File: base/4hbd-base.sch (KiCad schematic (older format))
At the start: 13 parts, among them J1 Screw_Terminal_01x03, J10 Screw_Terminal_01x04, J11 Screw_Terminal_01x02, J12 Conn_01x03, J13 Conn_01x08, J2 Screw_Terminal_01x03, J3 Screw_Terminal_01x03, J4 Screw_Terminal_01x03, J5 Screw_Terminal_01x02, J6 Screw_Terminal_01x02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

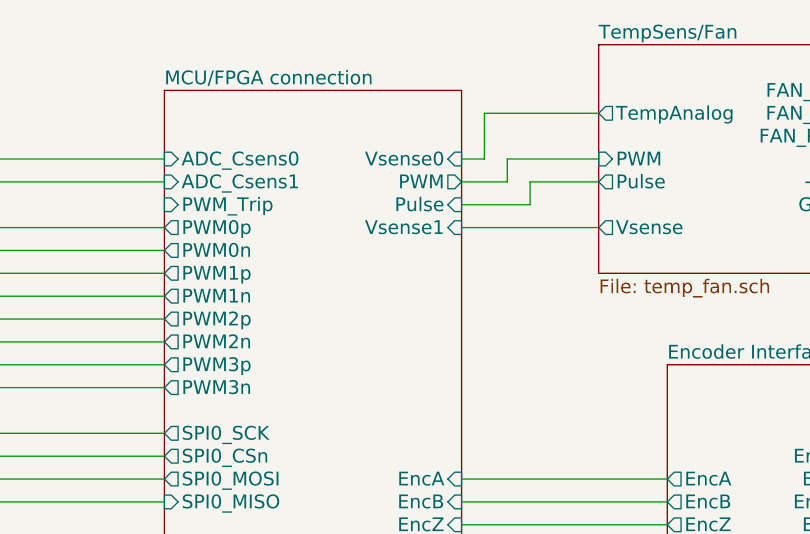
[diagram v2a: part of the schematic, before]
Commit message: Update base board: 1. Add extra analog voltage input to core board.   -> update pinmux 2. Assign most footprints. 3. Generate netlist. 4. Add core_sf board. 5. Add kicad_symbols library submodule.
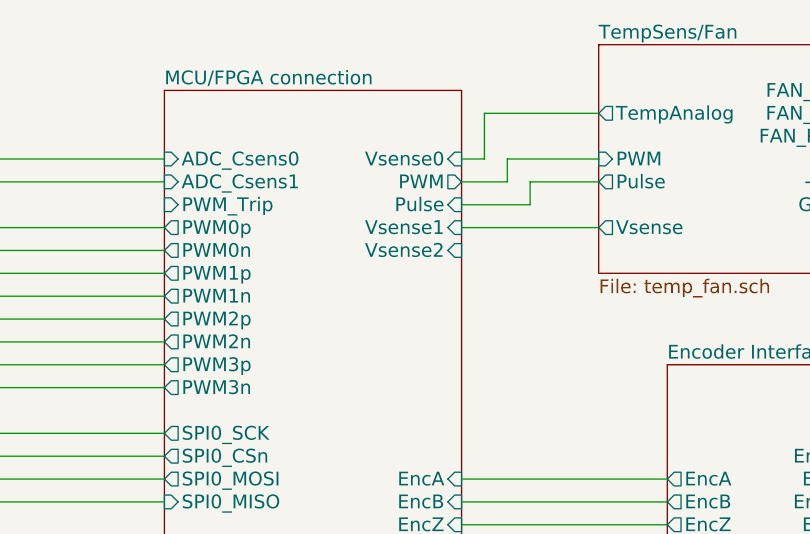
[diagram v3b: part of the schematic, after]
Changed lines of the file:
@@
 F40 "ADC_Csens1" I L 6900 1400 60
 F41 "ADC_Csens0" I L 6900 1300 60
+F42 "Vsense2" I R 8200 1700 60
 $EndSheet
 $Sheet
@@
 $EndSheet
 $Comp
-L GNDD #PWR8
+L GNDD #PWR01
 U 1 1 5A1C4DF7
 P 8900 6000
-F 0 "#PWR8" H 8900 5750 50  0001 C CNN
+F 0 "#PWR01" H 8900 5750 50  0001 C CNN
 F 1 "GNDD" H 8900 5875 50  0000 C CNN
 F 2 "" H 8900 6000 50  0001 C CNN
@@
 $EndComp
 $Comp
-L GNDD #PWR7
+L GNDD #PWR02
 U 1 1 5A1C5052
 P 8900 3500
-F 0 "#PWR7" H 8900 3250 50  0001 C CNN
+F 0 "#PWR02" H 8900 3250 50  0001 C CNN
 F 1 "GNDD" H 8900 3375 50  0000 C CNN
 F 2 "" H 8900 3500 50  0001 C CNN
@@
 $EndComp
 $Comp
-L GNDD #PWR5
+L GNDD #PWR03
 U 1 1 5A1C5445
 P 4800 5600
-F 0 "#PWR5" H 4800 5350 50  0001 C CNN
+F 0 "#PWR03" H 4800 5350 50  0001 C CNN
 F 1 "GNDD" H 4800 5475 50  0000 C CNN
 F 2 "" H 4800 5600 50  0001 C CNN
@@
 $EndComp
 $Comp
-L GNDD #PWR4
+L GNDD #PWR04
 U 1 1 5A1C7749
 P 4800 3800
-F 0 "#PWR4" H 4800 3550 50  0001 C CNN
+F 0 "#PWR04" H 4800 3550 50  0001 C CNN
 F 1 "GNDD" H 4800 3675 50  0000 C CNN
 F 2 "" H 4800 3800 50  0001 C CNN
@@
 $EndComp
 $Comp
-L GNDD #PWR6
+L GNDD #PWR05
 U 1 1 5A1D2700
 P 8400 4800
-F 0 "#PWR6" H 8400 4550 50  0001 C CNN
+F 0 "#PWR05" H 8400 4550 50  0001 C CNN
 F 1 "GNDD" H 8400 4675 50  0000 C CNN
 F 2 "" H 8400 4800 50  0001 C CNN
@@
 $EndComp
 $Comp
-L GNDD #PWR10
+L GNDD #PWR06
 U 1 1 5A1D7E7F
 P 10500 5500
-F 0 "#PWR10" H 10500 5250 50  0001 C CNN
+F 0 "#PWR06" H 10500 5250 50  0001 C CNN
 F 1 "GNDD" H 10500 5375 50  0000 C CNN
 F 2 "" H 10500 5500 50  0001 C CNN
@@
 $EndComp
 $Comp
-L GNDD #PWR11
+L GNDD #PWR07
 U 1 1 5A1E3D1F
 P 10600 2500
-F 0 "#PWR11" H 10600 2250 50  0001 C CNN
+F 0 "#PWR07" H 10600 2250 50  0001 C CNN
 F 1 "GNDD" H 10600 2375 50  0000 C CNN
 F 2 "" H 10600 2500 50  0001 C CNN
@@
 $EndComp
 $Comp
-L GNDD #PWR9
+L GNDD #PWR08
 U 1 1 5A1E950D
 P 10200 1600
-F 0 "#PWR9" H 10200 1350 50  0001 C CNN
+F 0 "#PWR08" H 10200 1350 50  0001 C CNN
 F 1 "GNDD" H 10200 1475 50  0000 C CNN
 F 2 "" H 10200 1600 50  0001 C CNN
@@
 	1200 7000 1400 7000
 $Comp
-L GNDPWR #PWR3
+L GNDPWR #PWR09
 U 1 1 5A1F43A1
 P 2800 5600
-F 0 "#PWR3" H 2800 5400 50  0001 C CNN
+F 0 "#PWR09" H 2800 5400 50  0001 C CNN
 F 1 "GNDPWR" H 2800 5470 50  0000 C CNN
 F 2 "" H 2800 5550 50  0001 C CNN
@@
 $EndComp
 $Comp
-L GNDPWR #PWR1
+L GNDPWR #PWR010
 U 1 1 5A1F4674
 P 1200 7100
-F 0 "#PWR1" H 1200 6900 50  0001 C CNN
+F 0 "#PWR010" H 1200 6900 50  0001 C CNN
 F 1 "GNDPWR" H 1200 6970 50  0000 C CNN
 F 2 "" H 1200 7050 50  0001 C CNN
@@
 $EndComp
 $Comp
-L GNDPWR #PWR2
+L GNDPWR #PWR011
 U 1 1 5A1F4ECF
 P 2800 3600
-F 0 "#PWR2" H 2800 3400 50  0001 C CNN
+F 0 "#PWR011" H 2800 3400 50  0001 C CNN
 F 1 "GNDPWR" H 2800 3470 50  0000 C CNN
 F 2 "" H 2800 3550 50  0001 C CNN
@@
 	6200 7200 6200 7400
 $Comp
-L GNDD #PWR?
+L GNDD #PWR012
 U 1 1 5A3B40B0
 P 6200 7400
-F 0 "#PWR?" H 6200 7150 50  0001 C CNN
+F 0 "#PWR012" H 6200 7150 50  0001 C CNN
 F 1 "GNDD" H 6200 7275 50  0000 C CNN
 F 2 "" H 6200 7400 50  0001 C CNN
@@
 $EndComp
 $Comp
-L GNDD #PWR?
+L GNDD #PWR013
 U 1 1 5A3B43A6
 P 4600 7000
-F 0 "#PWR?" H 4600 6750 50  0001 C CNN
+F 0 "#PWR013" H 4600 6750 50  0001 C CNN
 F 1 "GNDD" H 4600 6875 50  0000 C CNN
 F 2 "" H 4600 7000 50  0001 C CNN

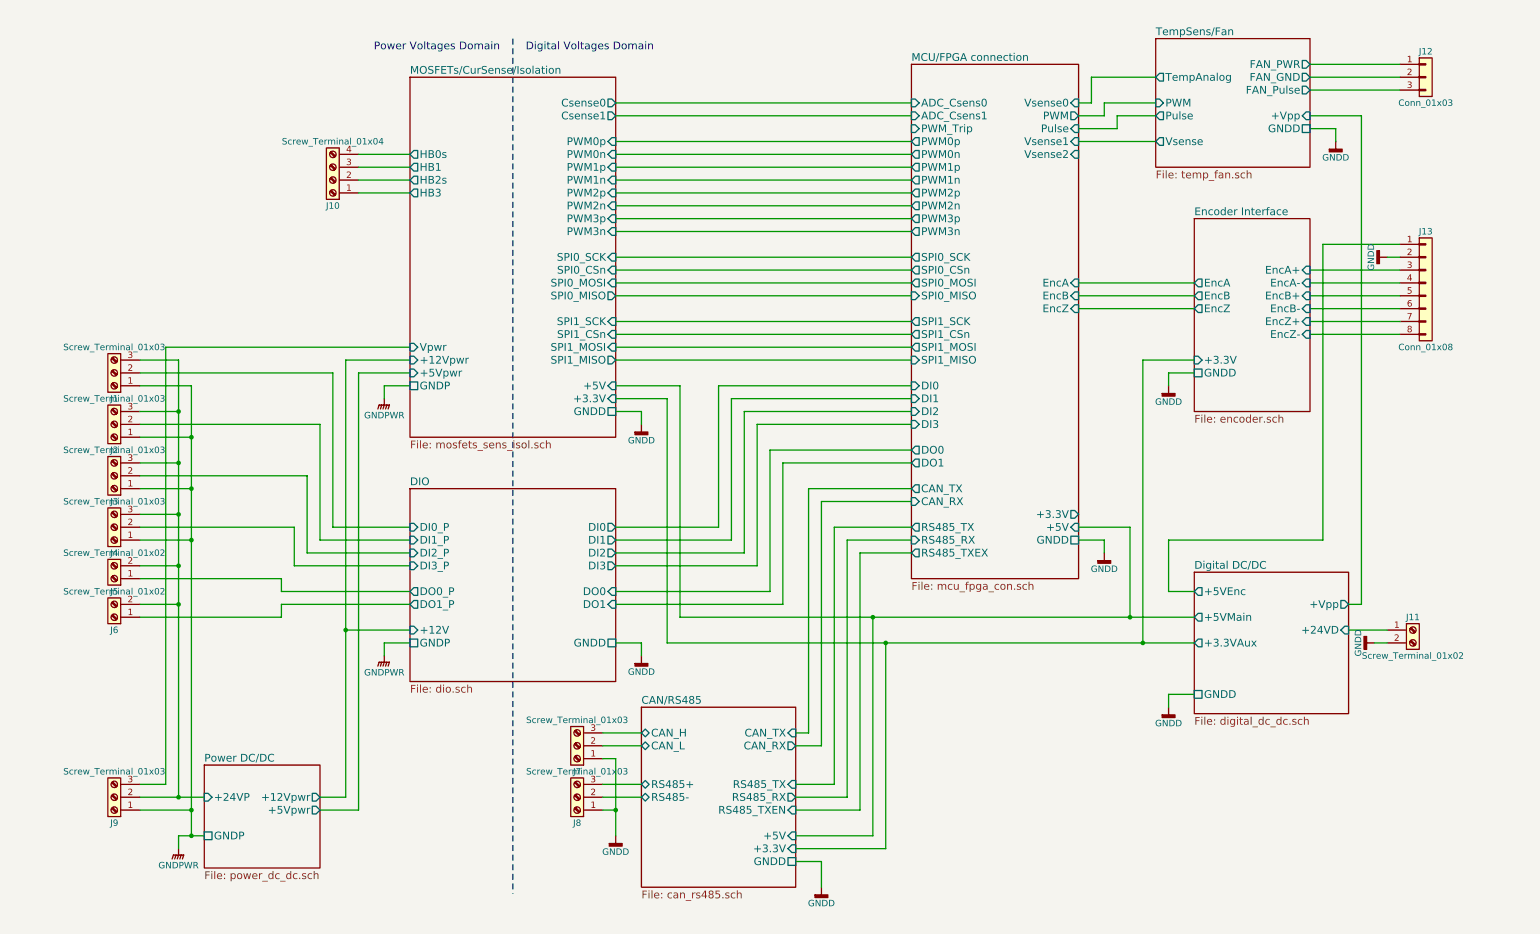
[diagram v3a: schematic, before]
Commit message: temp-sens-fan was created
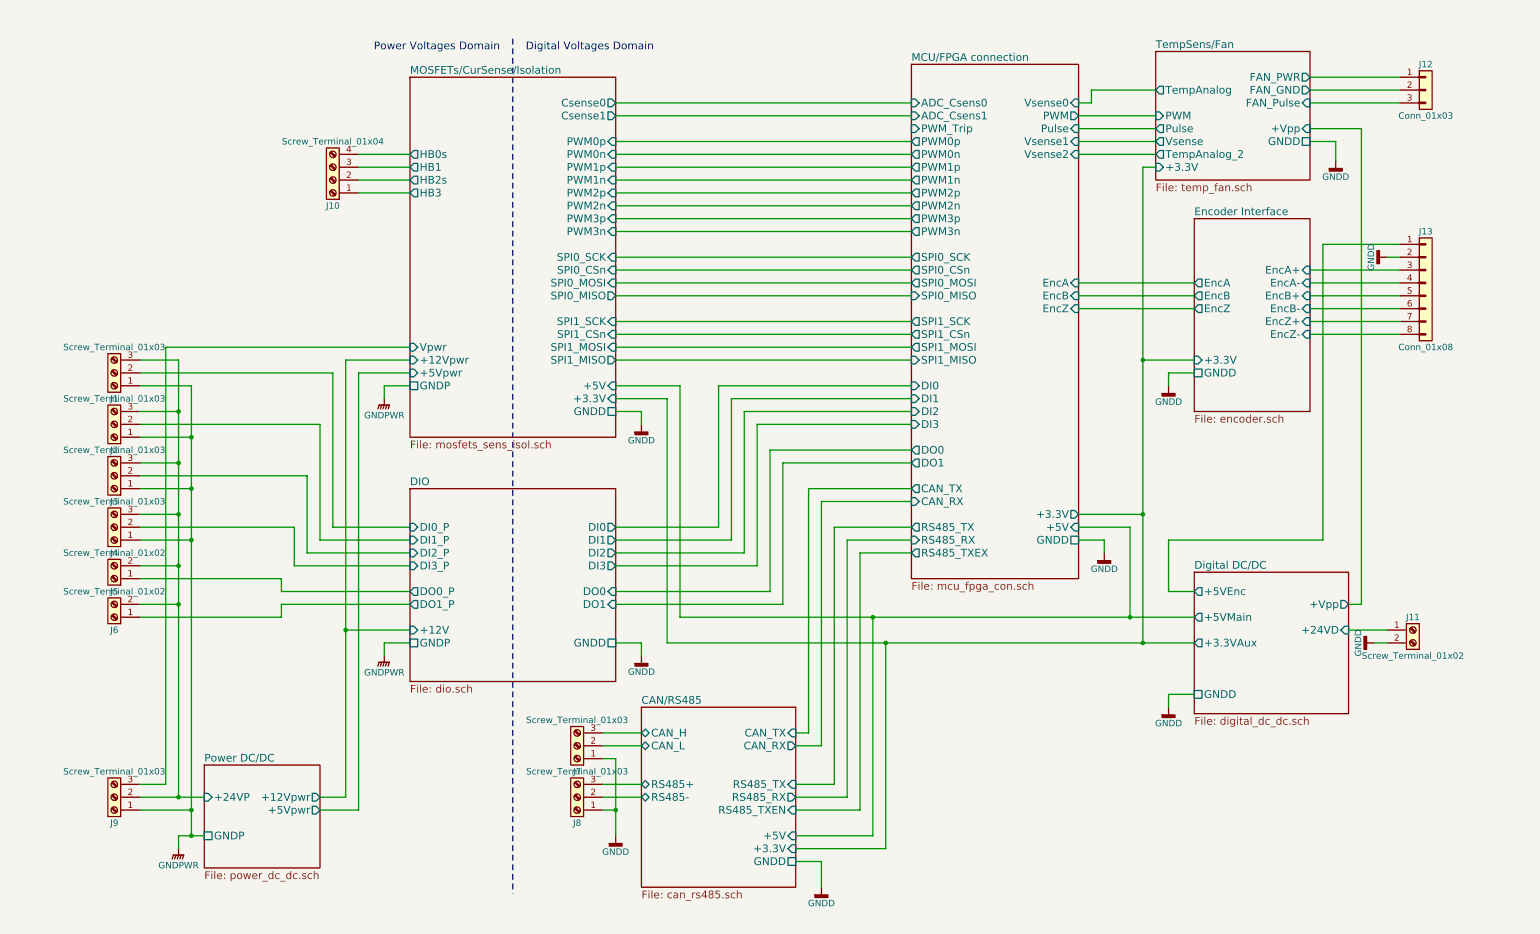
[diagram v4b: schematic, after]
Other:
- moved on the sheet: J12

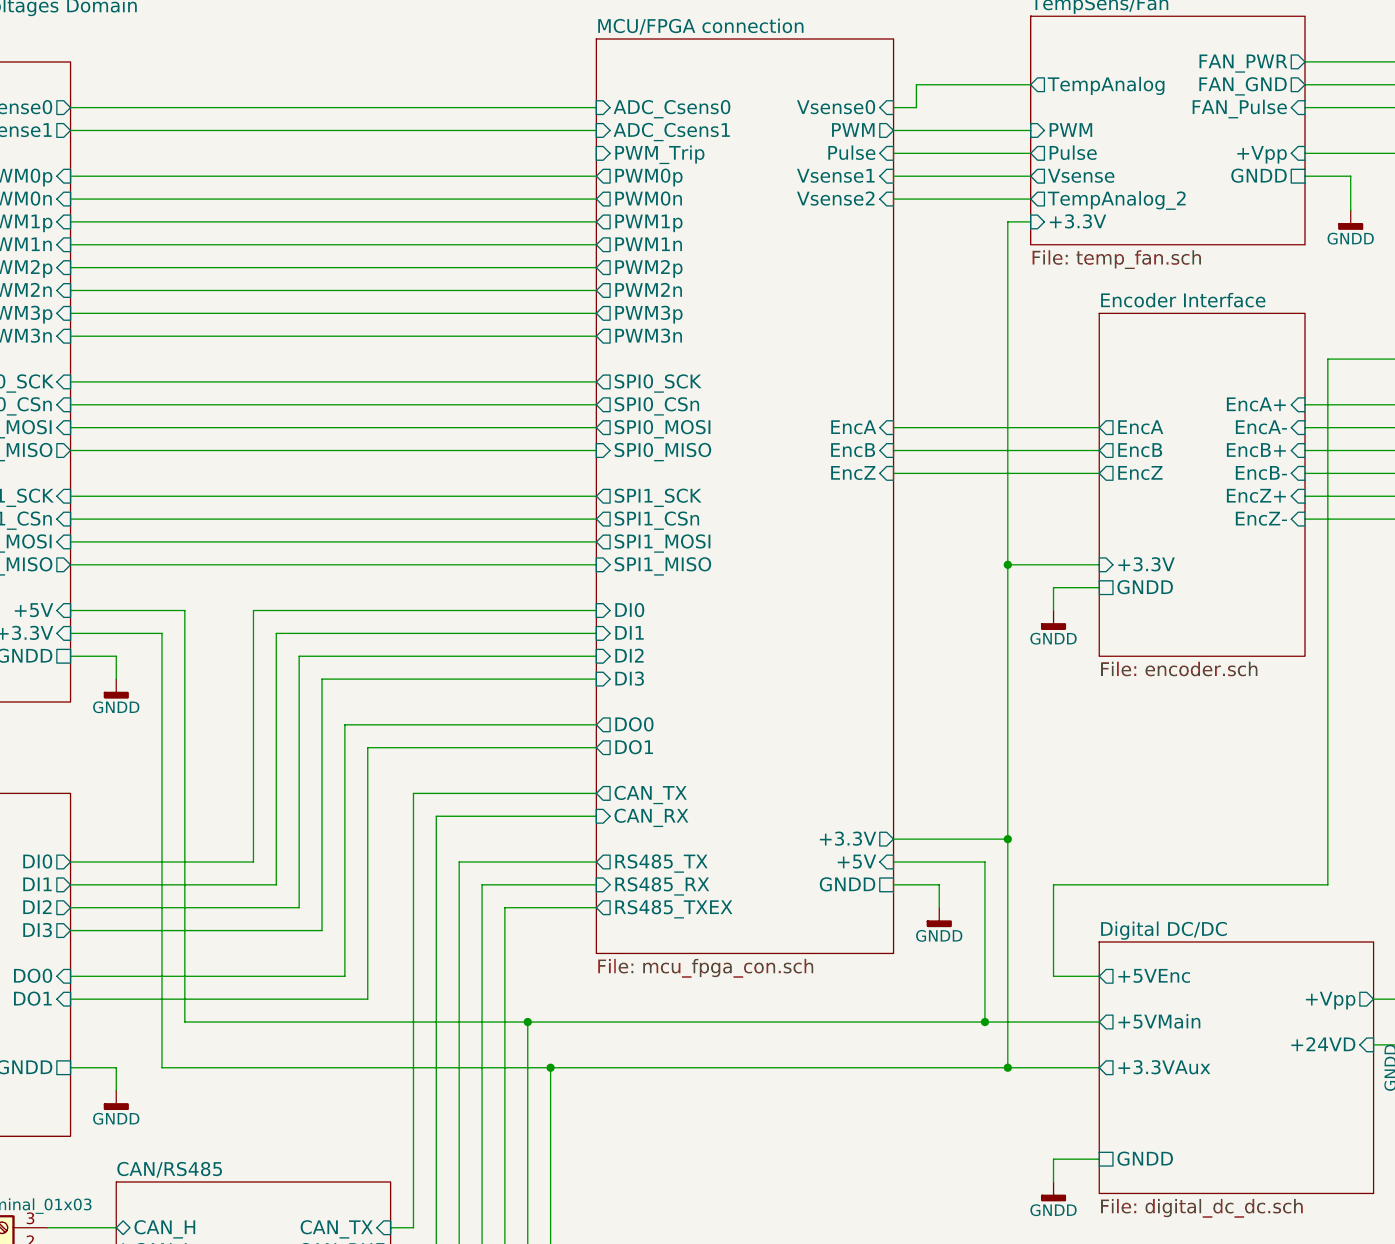
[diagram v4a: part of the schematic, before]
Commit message: Update footprints.
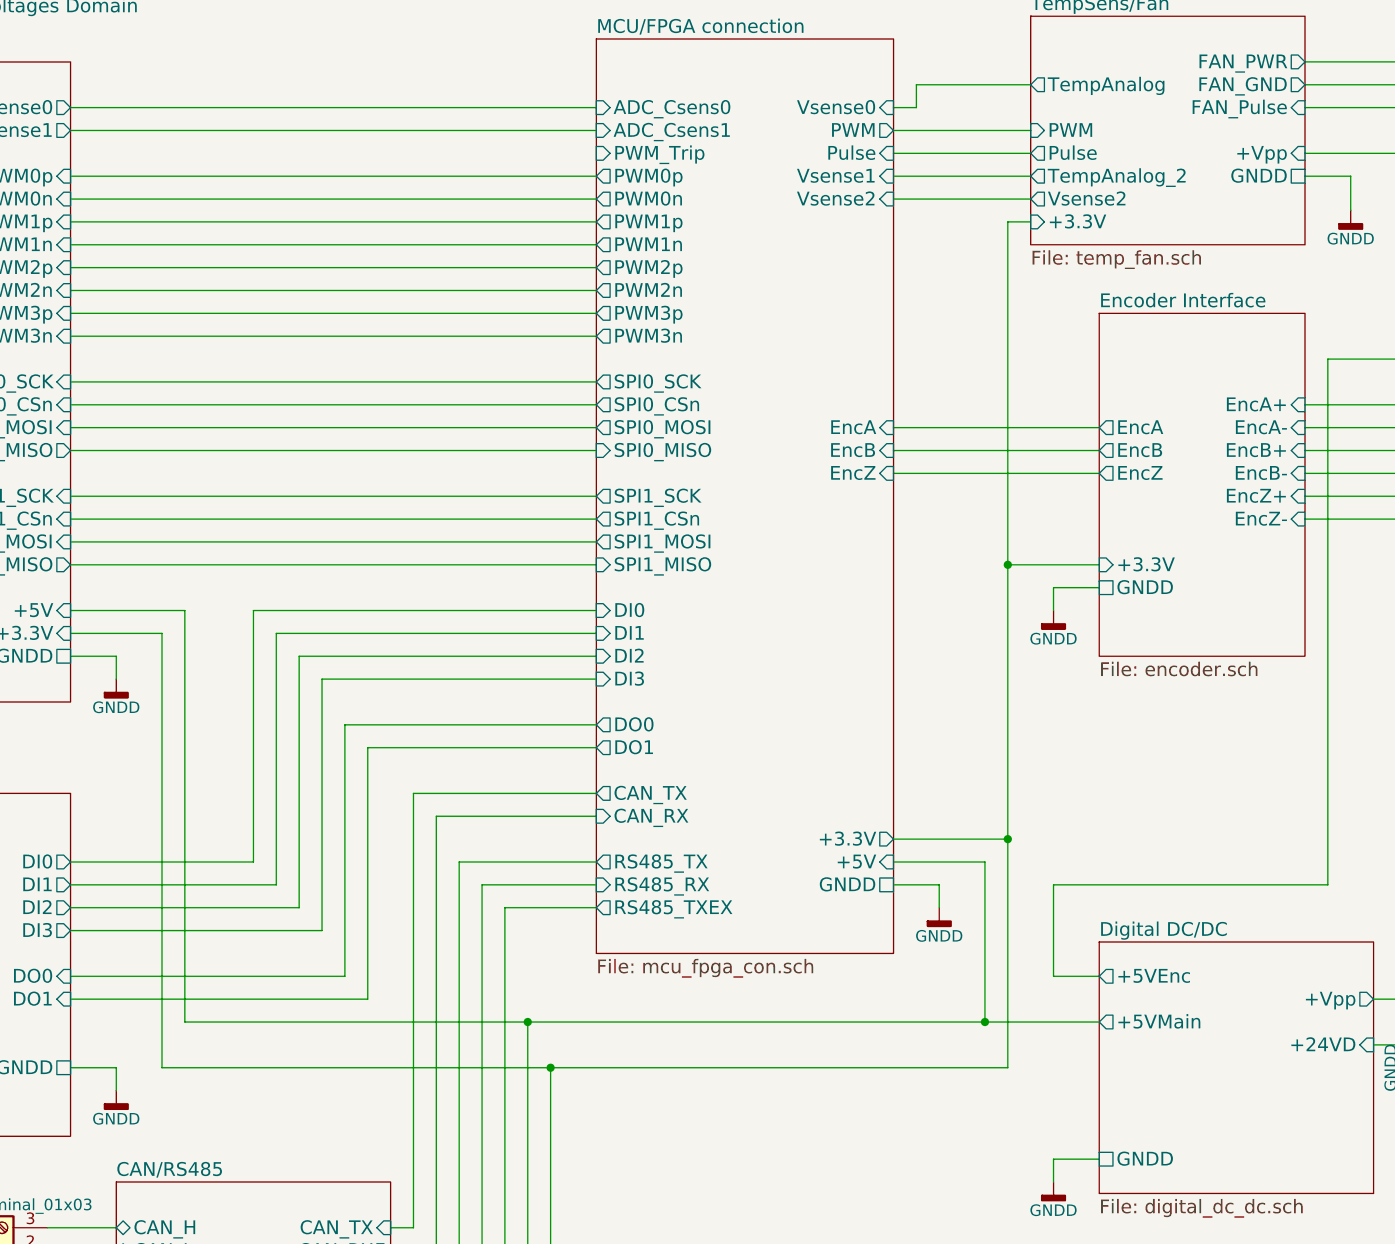
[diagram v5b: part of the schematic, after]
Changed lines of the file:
@@
 F8 "+Vpp" I R 10000 1500 60
 F9 "GNDD" U R 10000 1600 60
-F10 "Vsense" O L 8800 1600 60
-F11 "TempAnalog_2" O L 8800 1700 60
+F11 "TempAnalog_2" O L 8800 1600 60
 F12 "+3.3V" I L 8800 1800 60
+F13 "Vsense2" O L 8800 1700 60
 $EndSheet
 $Sheet
@@
 F3 "+5VEnc" O L 9100 5100 60
 F4 "+5VMain" O L 9100 5300 60
-F5 "+3.3VAux" O L 9100 5500 60
 F6 "GNDD" U L 9100 5900 60
 F7 "+Vpp" O R 10300 5200 60
@@
 Wire Wire Line
 	8700 1800 8700 5500
-Connection ~ 8700 5500
 Wire Wire Line
 	9100 2700 8200 2700
@@
 Wire Wire Line
 	5900 4100 6900 4100
-Wire Wire Line
-	5000 5500 9100 5500
 Wire Wire Line
 	4600 2800 6900 2800
@@
 	8200 4500 8700 4500
 Connection ~ 8700 4500
+Wire Wire Line
+	5000 5500 8700 5500
 $EndSCHEMATC
